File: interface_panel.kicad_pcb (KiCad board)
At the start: 2 copper layers, 50.6 x 29.8 mm, 13 parts, among them J1 Conn_02x04_Odd_Even

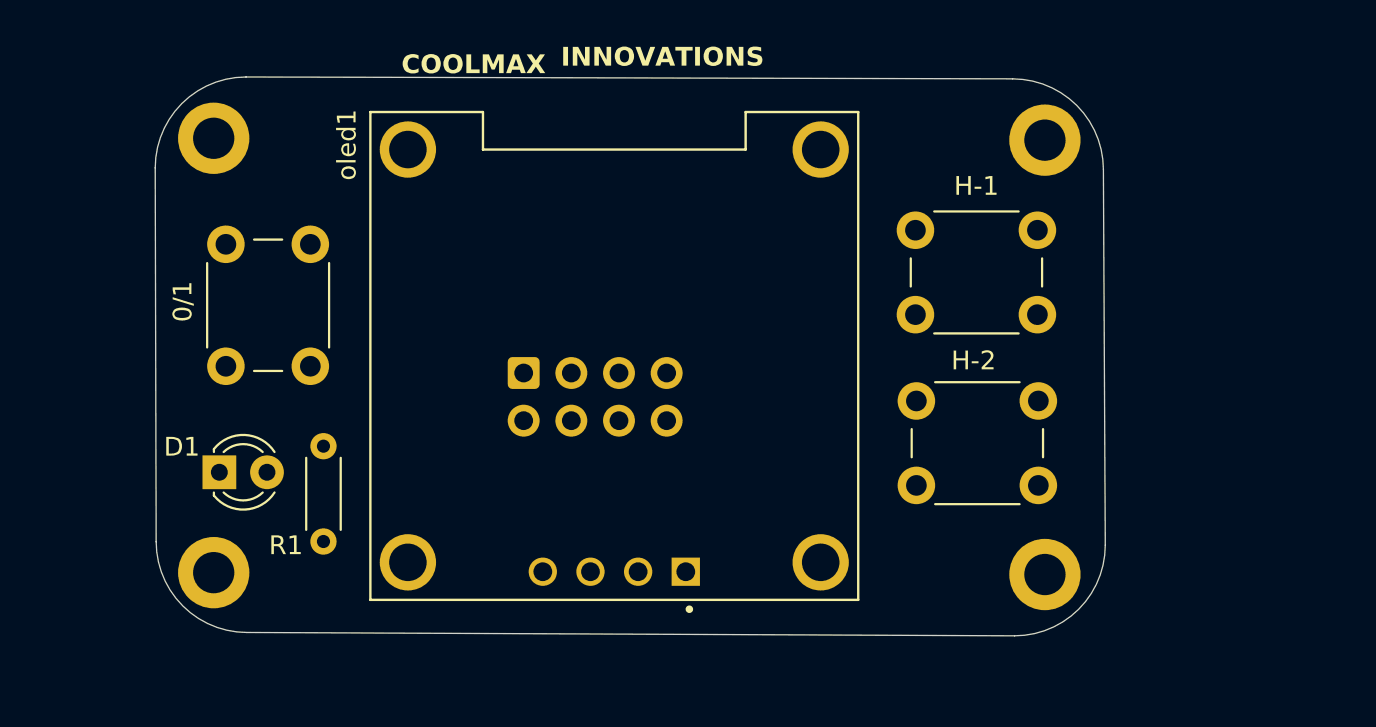
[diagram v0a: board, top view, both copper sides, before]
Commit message: changed layout with 12mm push_but
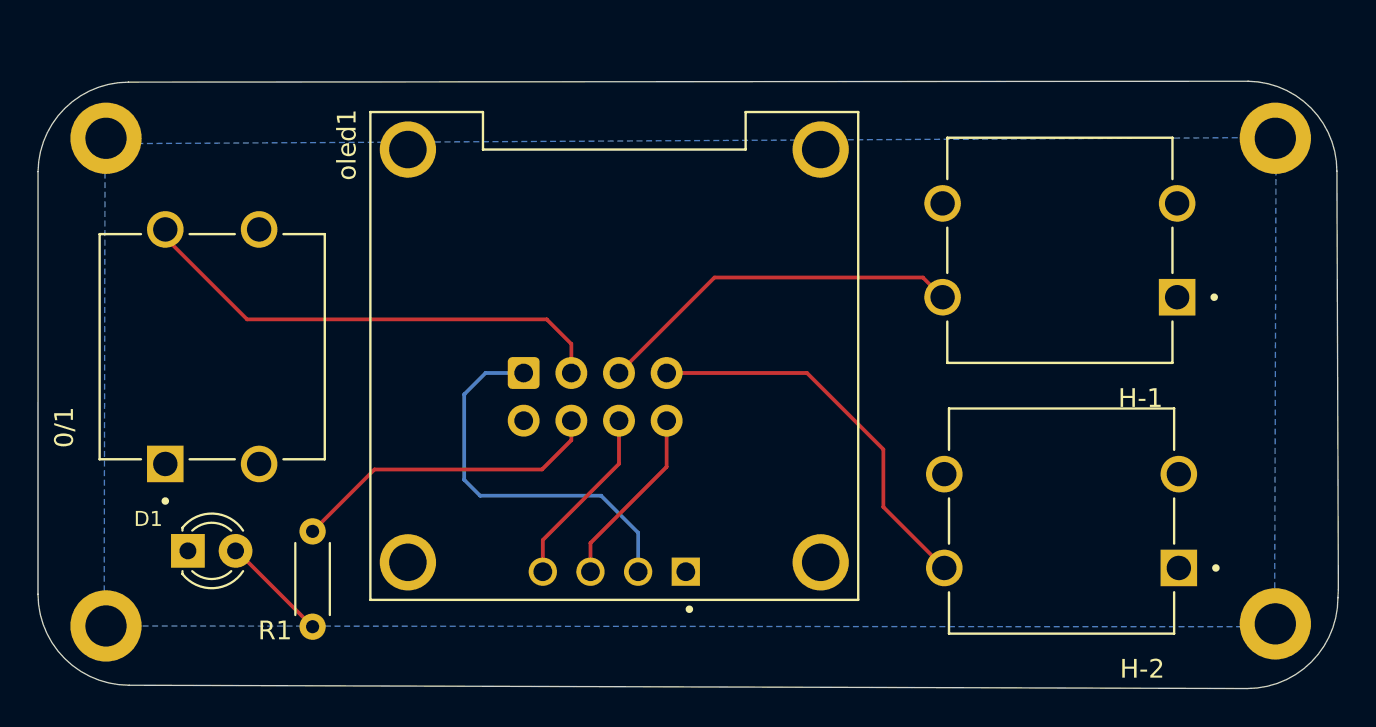
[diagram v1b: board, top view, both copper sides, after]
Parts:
- 0/1, H-1, H-2: footprint Button_Switch_THT:SW_PUSH_6mm -> pushbutt_12x12x7.3:SW_TS14-1212-140-BK-160-SCR-D
- moved REF** 12.6 mm to (178.3, 89.4)
- moved REF** 12.3 mm to (178.3, 63.5)
- moved 0/1 7.56 mm to (121.6, 74.7), turned to 90 degrees
- moved REF** 6.40 mm to (116.0, 89.5)
- moved REF** 5.74 mm to (116.0, 63.5)
- moved R1 4.58 mm to (127.0, 89.6)
- moved D1 4.51 mm to (120.3, 85.5)
- moved H-1 3.63 mm to (166.8, 69.5)
- moved H-2 2.27 mm to (166.9, 84.0)
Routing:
- net BT-Pwr: track 0.00 -> 26.0 mm
- net BT-2: track 0.00 -> 20.9 mm
- net 5V: track 0.00 -> 20.7 mm
- net BT-1: track 0.00 -> 19.8 mm
- net S. LED: track 0.00 -> 16.8 mm
- net SDA: track 0.00 -> 9.73 mm
- net SCL: track 0.00 -> 9.73 mm
- added copper zone on B.Cu, net GND
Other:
- board size 50.6 x 29.8 mm -> 69.3 x 32.4 mm

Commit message: production level changes -1
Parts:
- removed the REF** at (178.3, 63.5)
- removed the REF** at (116.0, 63.5)
- removed the REF** at (178.3, 89.4)
- removed the REF** at (151.6, 62.5)
- removed the REF** at (116.0, 89.5)
- removed the REF** at (161.1, 63.2)
- added C1: C, Capacitor_THT:C_Disc_D3.0mm_W1.6mm_P2.50mm, F.Cu at (192.8, 97.1)
- added C2: C, Capacitor_THT:C_Disc_D3.0mm_W1.6mm_P2.50mm, F.Cu at (197.9, 97.1)
- added J2: but1, Connector_JST:JST_EH_B2B-EH-A_1x02_P2.50mm_Vertical, F.Cu at (134.5, 96.6)
- added J3: but2, Connector_JST:JST_EH_B2B-EH-A_1x02_P2.50mm_Vertical, F.Cu at (134.5, 70.6)
- added J4: but3, Connector_JST:JST_EH_B2B-EH-A_1x02_P2.50mm_Vertical, F.Cu at (221.6, 97.0)
- added J5: Led, Connector_JST:JST_EH_B2B-EH-A_1x02_P2.50mm_Vertical, F.Cu at (227.6, 96.0)
- added R2: 10k, Resistor_THT:R_Axial_DIN0204_L3.6mm_D1.6mm_P5.08mm_Horizontal, F.Cu at (173.6, 97.4)
- added REF**: MountingHole_2mm, MountingHole:MountingHole_2mm, F.Cu at (233.8, 97.6)
- added REF**: MountingHole_2mm, MountingHole:MountingHole_2mm, F.Cu at (128.5, 97.6)
- added REF**: MountingHole_2mm, MountingHole:MountingHole_2mm, F.Cu at (233.8, 70.1)
- added REF**: MountingHole_2mm, MountingHole:MountingHole_2mm, F.Cu at (128.5, 70.1)
- added U2: ATmega328P-P, Package_DIP:DIP-28_W7.62mm, F.Cu at (172.5, 93.9)
- added Y1: Crystal, Crystal:Crystal_HC18-U_Vertical, F.Cu at (210.9, 94.7)
- added reset1: reset, Button_Switch_THT:SW_PUSH_6mm, F.Cu at (223.1, 91.3)
- moved D1 106.7 mm to (227.1, 86.5)
- moved R1 105.9 mm to (232.8, 85.2), turned to -90 degrees
- moved 0/1 79.5 mm to (201.1, 76.5), turned to 0 degrees
- moved H-2 55.8 mm to (222.2, 76.5), turned to 0 degrees
- moved oled1 15.2 mm to (155.3, 84.1), turned to 0 degrees
- moved H-1 14.9 mm to (180.0, 76.5), turned to 0 degrees
- moved J1 4.78 mm to (135.7, 80.1), turned to 180 degrees
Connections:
- J1 pad 6: SDA -> RX
- J1 pad 8: SCL -> TX
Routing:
- net S. LED: track 16.8 -> 124.1 mm, vias 0 -> 2
- net BT-2: track 20.9 -> 109.9 mm, vias 0 -> 2
- net BT-Pwr: track 26.0 -> 98.3 mm, vias 0 -> 4
- net Net-(U2-~{RESET}/PC6): track 0.00 -> 59.7 mm
- net RX: track 0.00 -> 52.3 mm
- net TX: track 0.00 -> 48.0 mm
- net Net-(U2-XTAL2/PB7): track 0.00 -> 23.7 mm
- net Net-(U2-XTAL1/PB6): track 0.00 -> 23.5 mm
- net BT-1: track 19.8 -> 42.2 mm, vias 0 -> 2
- net 5V: track 20.7 -> 0.00 mm
- net SCL: track 9.73 -> 21.9 mm
- net SDA: track 9.73 -> 21.9 mm
- net Net-(D1-A): track 0.00 -> 3.76 mm
- removed copper zone on B.Cu, net GND
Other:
- board size 69.3 x 32.4 mm -> 111.2 x 33.4 mm

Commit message: production change-2
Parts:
- removed R2: 10k, Resistor_THT:R_Axial_DIN0204_L3.6mm_D1.6mm_P5.08mm_Horizontal
- removed REF** (x4): MountingHole_2mm, MountingHole:MountingHole_2mm
- removed reset1: reset, Button_Switch_THT:SW_PUSH_6mm
- added H1: MountingHole, MountingHole:MountingHole_2.2mm_M2, F.Cu at (128.7, 70.2)
- added H2: MountingHole, MountingHole:MountingHole_2.2mm_M2, F.Cu at (128.7, 97.3)
- added H3: MountingHole, MountingHole:MountingHole_2.2mm_M2, F.Cu at (233.6, 70.2)
- added H4: MountingHole, MountingHole:MountingHole_2.2mm_M2, F.Cu at (233.6, 97.3)
- J2, J3, J4, J5: moved to B.Cu
- moved R1 10.1 mm to (222.7, 85.4), turned to 0 degrees
- moved D1 10.1 mm to (216.9, 86.4)
- moved J4 2.40 mm to (219.2, 96.5), turned to 0 degrees
- moved J3 1.08 mm to (134.9, 71.6)
- moved J5 0.61 mm to (228.2, 95.9)
- moved J2 0.57 mm to (134.9, 97.0)
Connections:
- U2 pad 1: Net-(U2-~{RESET}/PC6) -> unconnected-(U2-~{RESET}/PC6-Pad1)
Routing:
- net 5V: track 0.00 -> 66.7 mm
- net Net-(U2-~{RESET}/PC6): track 59.7 -> 0.00 mm
- net BT-1: track 42.2 -> 56.1 mm
- net S. LED: track 124.1 -> 129.2 mm, vias 2 -> 0
- net BT-Pwr: track 98.3 -> 99.9 mm, vias 4 -> 2
- net BT-2: track 109.9 -> 108.5 mm
- added copper zone on B.Cu, net GND

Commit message: oled Production
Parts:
- removed J1: Conn_02x04_Odd_Even, Connector_IDC:IDC-Header_2x04_P2.54mm_Vertical
- added J6: Conn_01x02_Socket, Connector_PinHeader_1.27mm:PinHeader_1x02_P1.27mm_Vertical, F.Cu at (181.3, 97.7)
- added J7: Conn_02x05_Odd_Even, Connector_IDC:IDC-Header_2x05_P2.54mm_Vertical, B.Cu at (136.5, 78.7)
- added R2: 10k, Resistor_THT:R_Axial_DIN0204_L3.6mm_D1.6mm_P5.08mm_Horizontal, F.Cu at (172.6, 97.3)
- moved J2 22.8 mm to (149.4, 79.3), turned to 180 degrees
- moved J3 20.7 mm to (149.3, 86.5), turned to 180 degrees
- moved D1 2.57 mm to (217.1, 89.0)
- moved R1 2.41 mm to (222.9, 87.8)
- moved J4 1.13 mm to (220.4, 96.5), turned to 180 degrees
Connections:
- U2 pad 1: unconnected-(U2-~{RESET}/PC6-Pad1) -> Net-(J6-Pin_1)
- U2 pad 13: unconnected-(U2-PD7-Pad13) -> D7
- U2 pad 17: unconnected-(U2-PB3-Pad17) -> D11
- U2 pad 20: unconnected-(U2-AVCC-Pad20) -> 5V
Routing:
- net D7: track 0.00 -> 78.8 mm, vias 0 -> 2
- net D11: track 0.00 -> 68.0 mm, vias 0 -> 4
- net BT-2: track 108.5 -> 83.2 mm
- net 5V: track 66.7 -> 83.6 mm, vias 0 -> 1
- net BT-1: track 56.1 -> 41.3 mm, vias 2 -> 1
- net BT-Pwr: track 99.9 -> 113.5 mm, vias 2 -> 3
- net TX: track 48.0 -> 61.4 mm
- net Net-(J6-Pin_1): track 0.00 -> 10.5 mm
- net RX: track 52.3 -> 62.7 mm
- net S. LED: track 129.2 -> 135.0 mm, vias 0 -> 4

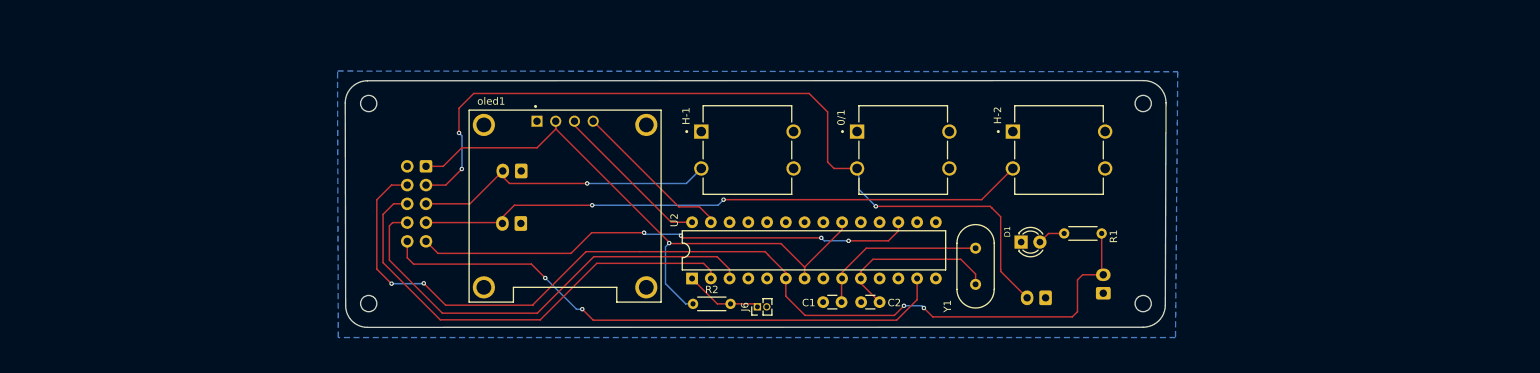
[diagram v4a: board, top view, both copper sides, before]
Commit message: 7segment added
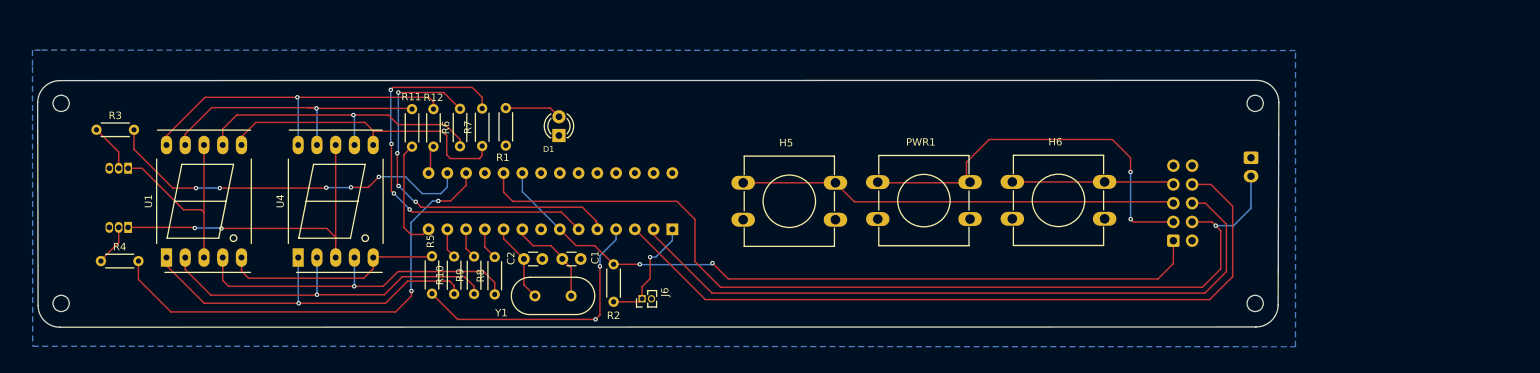
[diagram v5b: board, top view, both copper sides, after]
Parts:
- removed 0/1, H-1, H-2: SW_Push, pushbutt_12x12x7.3:SW_TS14-1212-140-BK-160-SCR-D
- removed J2: but1, Connector_JST:JST_EH_B2B-EH-A_1x02_P2.50mm_Vertical
- removed J3: but2, Connector_JST:JST_EH_B2B-EH-A_1x02_P2.50mm_Vertical
- removed J4: but3, Connector_JST:JST_EH_B2B-EH-A_1x02_P2.50mm_Vertical
- removed oled1: ~, oled0.9in:MODULE_DM-OLED096-636
- added H5: SW_Push, Button_Switch_THT:SW_PUSH-12mm, F.Cu at (179.4, 80.9)
- added H6: SW_Push, Button_Switch_THT:SW_PUSH-12mm, F.Cu at (215.9, 80.8)
- added PWR1: SW_Push, Button_Switch_THT:SW_PUSH-12mm, F.Cu at (197.7, 80.8)
- added Q1: 2n222a, Package_TO_SOT_THT:TO-92_Inline, B.Cu at (96.1, 79.0)
- added Q2: 2n222a, Package_TO_SOT_THT:TO-92_Inline, B.Cu at (96.1, 87.0)
- added R10: R, Resistor_THT:R_Axial_DIN0204_L3.6mm_D1.6mm_P5.08mm_Horizontal, F.Cu at (140.3, 96.0)
- added R11: R, Resistor_THT:R_Axial_DIN0204_L3.6mm_D1.6mm_P5.08mm_Horizontal, F.Cu at (134.6, 71.0)
- added R12: R, Resistor_THT:R_Axial_DIN0204_L3.6mm_D1.6mm_P5.08mm_Horizontal, F.Cu at (137.5, 71.0)
- added R3: R, Resistor_THT:R_Axial_DIN0204_L3.6mm_D1.6mm_P5.08mm_Horizontal, F.Cu at (91.8, 73.8)
- added R4: R, Resistor_THT:R_Axial_DIN0204_L3.6mm_D1.6mm_P5.08mm_Horizontal, F.Cu at (92.4, 91.5)
- added R5: R, Resistor_THT:R_Axial_DIN0204_L3.6mm_D1.6mm_P5.08mm_Horizontal, F.Cu at (137.3, 90.9)
- added R6: R, Resistor_THT:R_Axial_DIN0204_L3.6mm_D1.6mm_P5.08mm_Horizontal, F.Cu at (141.1, 76.0)
- added R7: R, Resistor_THT:R_Axial_DIN0204_L3.6mm_D1.6mm_P5.08mm_Horizontal, F.Cu at (144.1, 76.0)
- added R8: R, Resistor_THT:R_Axial_DIN0204_L3.6mm_D1.6mm_P5.08mm_Horizontal, F.Cu at (145.8, 96.1)
- added R9: R, Resistor_THT:R_Axial_DIN0204_L3.6mm_D1.6mm_P5.08mm_Horizontal, F.Cu at (143.0, 96.0)
- added U1: SM420561N, Display_7Segment:7SegmentLED_LTS6760_LTS6780, F.Cu at (101.3, 91.1)
- added U4: SM420561N, Display_7Segment:7SegmentLED_LTS6760_LTS6780, F.Cu at (119.2, 91.1)
- U2: moved to B.Cu
- moved J7 101.7 mm to (237.7, 88.8), turned to 0 degrees
- moved R1 77.5 mm to (147.3, 70.8), turned to -90 degrees
- moved D1 64.2 mm to (154.5, 74.5), turned to 90 degrees
- moved Y1 59.7 mm to (151.2, 96.3), turned to 0 degrees
- moved C2 48.5 mm to (149.7, 91.3), turned to 0 degrees
- moved H1 41.7 mm to (87.0, 70.2)
- moved H2 41.7 mm to (87.0, 97.3)
- moved C1 38.3 mm to (154.9, 91.3), turned to 0 degrees
- moved J5 27.2 mm to (248.2, 77.5), turned to -90 degrees
- moved J6 15.7 mm to (165.7, 96.7)
- moved H3 15.2 mm to (248.8, 70.2)
- moved H4 15.2 mm to (248.8, 97.3)
- moved R2 12.0 mm to (161.9, 92.0), turned to -90 degrees
- moved U2 7.18 mm to (169.8, 87.2)
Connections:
- J7 pad 9: D11 -> D12
- U2 pad 11: unconnected-(U2-PD5-Pad11) -> Net-(U2-PD5)
- U2 pad 12: unconnected-(U2-PD6-Pad12) -> Net-(U2-PD6)
- U2 pad 13: D7 -> Net-(U2-PD7)
- U2 pad 14: unconnected-(U2-PB0-Pad14) -> Net-(U2-PB0)
- U2 pad 15: unconnected-(U2-PB1-Pad15) -> Net-(U2-PB1)
- U2 pad 16: unconnected-(U2-PB2-Pad16) -> CC1
- U2 pad 17: D11 -> CC2
- U2 pad 18: unconnected-(U2-PB4-Pad18) -> D12
- U2 pad 19: unconnected-(U2-PB5-Pad19) -> S. LED
- U2 pad 27: SDA -> unconnected-(U2-PC4-Pad27)
- U2 pad 28: SCL -> unconnected-(U2-PC5-Pad28)
- U2 pad 4: unconnected-(U2-PD2-Pad4) -> Net-(U2-PD2)
- U2 pad 5: unconnected-(U2-PD3-Pad5) -> Net-(U2-PD3)
- U2 pad 6: S. LED -> Net-(U2-PD4)
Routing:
- net D7: track 78.8 -> 0.00 mm, vias 2 -> 0
- net D11: track 68.0 -> 0.00 mm, vias 4 -> 0
- net CC2: track 0.00 -> 63.4 mm, vias 0 -> 2
- net BT-2: track 83.2 -> 22.9 mm, vias 2 -> 0
- net BT-Pwr: track 113.5 -> 55.2 mm, vias 3 -> 2
- net Net-(U2-PD4): track 0.00 -> 55.9 mm, vias 0 -> 4
- net Net-(U2-PD3): track 0.00 -> 52.0 mm, vias 0 -> 4
- net CC1: track 0.00 -> 51.3 mm, vias 0 -> 5
- net E: track 0.00 -> 51.1 mm, vias 0 -> 1
- net D: track 0.00 -> 49.9 mm, vias 0 -> 1
- net C: track 0.00 -> 47.3 mm, vias 0 -> 1
- net G: track 0.00 -> 47.2 mm, vias 0 -> 1
- net Net-(Q2-C): track 0.00 -> 43.9 mm, vias 0 -> 2
- net B: track 0.00 -> 42.4 mm
- net A: track 0.00 -> 41.7 mm, vias 0 -> 1
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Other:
- board size 111.2 x 33.4 mm -> 168.1 x 33.4 mm

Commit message: Segment-added
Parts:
- Q1, Q2: value 2n222a -> BC547
- Y1: moved to B.Cu
- moved R8 25.1 mm to (144.2, 71.0), turned to -90 degrees
- moved R11 20.7 mm to (140.2, 90.9)
- moved R6 20.3 mm to (137.3, 95.9)
- moved R5 14.8 mm to (137.4, 76.1), turned to 90 degrees
- moved R12 6.05 mm to (134.4, 76.2), turned to 90 degrees
- moved R9 5.89 mm to (145.8, 90.8), turned to -90 degrees
- moved R10 5.78 mm to (143.0, 90.9), turned to -90 degrees
- moved R7 5.66 mm to (141.3, 71.0), turned to -90 degrees
- moved R4 5.15 mm to (97.6, 91.7), turned to 180 degrees
- moved R3 5.07 mm to (96.9, 73.5), turned to 180 degrees
- moved H5 0.49 mm to (178.9, 81.0)
- moved Y1 0.08 mm to (151.2, 96.3)
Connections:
- J7 pad 9: D12 -> D11
- Q1 pad 2: Net-(Q1-B) -> CC1
- Q2 pad 2: Net-(Q2-B) -> CC2
- R10 pad 1: E -> Net-(U2-PD6)
- R10 pad 2: Net-(U2-PD7) -> D
- R11 pad 1: F -> Net-(U2-PD7)
- R11 pad 2: Net-(U2-PB0) -> E
- R12 pad 1: G -> Net-(U2-PB0)
- R12 pad 2: Net-(U2-PB1) -> F
- R3 pad 1: Net-(Q1-B) -> Net-(U2-PB2)
- R4 pad 1: Net-(Q2-B) -> Net-(U2-PB3)
- R5 pad 1: DP -> Net-(U2-PB1)
- R5 pad 2: Net-(U2-PD2) -> G
- R6 pad 1: A -> Net-(U2-PD2)
- R6 pad 2: Net-(U2-PD3) -> DPX
- R7 pad 1: B -> Net-(U2-PD3)
- R7 pad 2: Net-(U2-PD4) -> A
- R8 pad 1: C -> Net-(U2-PD4)
- R8 pad 2: Net-(U2-PD5) -> B
- R9 pad 1: D -> Net-(U2-PD5)
- R9 pad 2: Net-(U2-PD6) -> C
- U1 pad 5: DP -> DPX
- U2 pad 16: CC1 -> Net-(U2-PB2)
- U2 pad 17: CC2 -> Net-(U2-PB3)
- U4 pad 5: DP -> DPX
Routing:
- net Net-(U2-PB3): track 0.00 -> 63.4 mm, vias 0 -> 2
- net CC2: track 63.4 -> 5.56 mm, vias 2 -> 0
- net Net-(U2-PB2): track 0.00 -> 51.3 mm, vias 0 -> 5
- net CC1: track 51.3 -> 6.46 mm, vias 5 -> 0
- net DPX: track 0.00 -> 30.2 mm
- net DP: track 30.2 -> 0.00 mm
- net Net-(Q1-B): track 6.46 -> 0.00 mm
- net Net-(Q2-B): track 5.56 -> 0.00 mm
- net S. LED: track 129.1 -> 132.9 mm
- net F: track 39.8 -> 38.7 mm
- net BT-1: track 59.4 -> 60.4 mm
- net Net-(U2-PD2): vias 2 -> 1

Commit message: updated
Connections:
- J7 pad 9: D11 -> D13
- U2 pad 18: D12 -> S. LED
- U2 pad 19: S. LED -> D13
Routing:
- net D13: track 0.00 -> 96.3 mm
- net S. LED: track 132.9 -> 136.2 mm

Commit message: updated
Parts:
- added J1: B1, Connector_JST:JST_EH_B2B-EH-A_1x02_P2.50mm_Vertical, B.Cu at (190.0, 71.2)
- added J2: B2, Connector_JST:JST_EH_B2B-EH-A_1x02_P2.50mm_Vertical, B.Cu at (251.1, 71.2)
- added J3: BP, Connector_JST:JST_EH_B2B-EH-A_1x02_P2.50mm_Vertical, B.Cu at (221.1, 71.2)
- added JP1: sda, Jumper:SolderJumper-2_P1.3mm_Open_Pad1.0x1.5mm, B.Cu at (166.8, 83.3)
- added JP2: scl, Jumper:SolderJumper-2_P1.3mm_Open_Pad1.0x1.5mm, B.Cu at (164.1, 83.3)
- added R13: R, Resistor_THT:R_Axial_DIN0204_L3.6mm_D1.6mm_P5.08mm_Horizontal, F.Cu at (89.3, 81.5)
- added R14: R, Resistor_THT:R_Axial_DIN0204_L3.6mm_D1.6mm_P5.08mm_Horizontal, F.Cu at (89.3, 85.6)
- moved H2 193.6 mm to (280.6, 97.3)
- moved H4 161.7 mm to (87.0, 97.3)
- moved H3 31.8 mm to (280.6, 70.2)
- moved J7 30.6 mm to (268.3, 88.6)
- moved J5 30.6 mm to (278.8, 79.3)
- moved H6 27.6 mm to (243.5, 81.7)
- moved PWR1 15.5 mm to (213.2, 81.7)
- moved H5 3.96 mm to (182.8, 81.7)
- moved D1 2.35 mm to (156.7, 73.7), turned to 180 degrees
- moved R4 1.15 mm to (97.6, 92.9)
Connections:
- U2 pad 27: unconnected-(U2-PC4-Pad27) -> Net-(JP1-A)
- U2 pad 28: unconnected-(U2-PC5-Pad28) -> Net-(JP2-A)
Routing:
- net BT-1: track 60.4 -> 106.5 mm, vias 0 -> 2
- net TX: track 102.5 -> 137.0 mm
- net RX: track 95.0 -> 129.4 mm
- net S. LED: track 136.2 -> 165.4 mm
- net D13: track 96.3 -> 125.3 mm
- net 5V: track 99.7 -> 128.6 mm
- net BT-Pwr: track 55.2 -> 77.7 mm, vias 2 -> 0
- net BT-2: track 22.9 -> 37.8 mm
- net Net-(JP2-A): track 0.00 -> 7.35 mm, vias 0 -> 1
- net CC2: track 5.56 -> 11.9 mm
- net CC1: track 6.46 -> 11.6 mm
- net Net-(JP1-A): track 0.00 -> 3.25 mm
- net Net-(U2-PB3): track 63.4 -> 62.0 mm
- net Net-(D1-A): track 7.69 -> 8.46 mm
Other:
- board size 168.1 x 33.4 mm -> 199.9 x 33.4 mm
